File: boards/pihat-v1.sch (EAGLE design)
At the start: 53 parts, among them J10 RASPBERRYPI-40-PIN-GPIO_PTH_N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, Q1 BSS138, Q13 BSS138, Q2 BSS138, Q3 BSS138

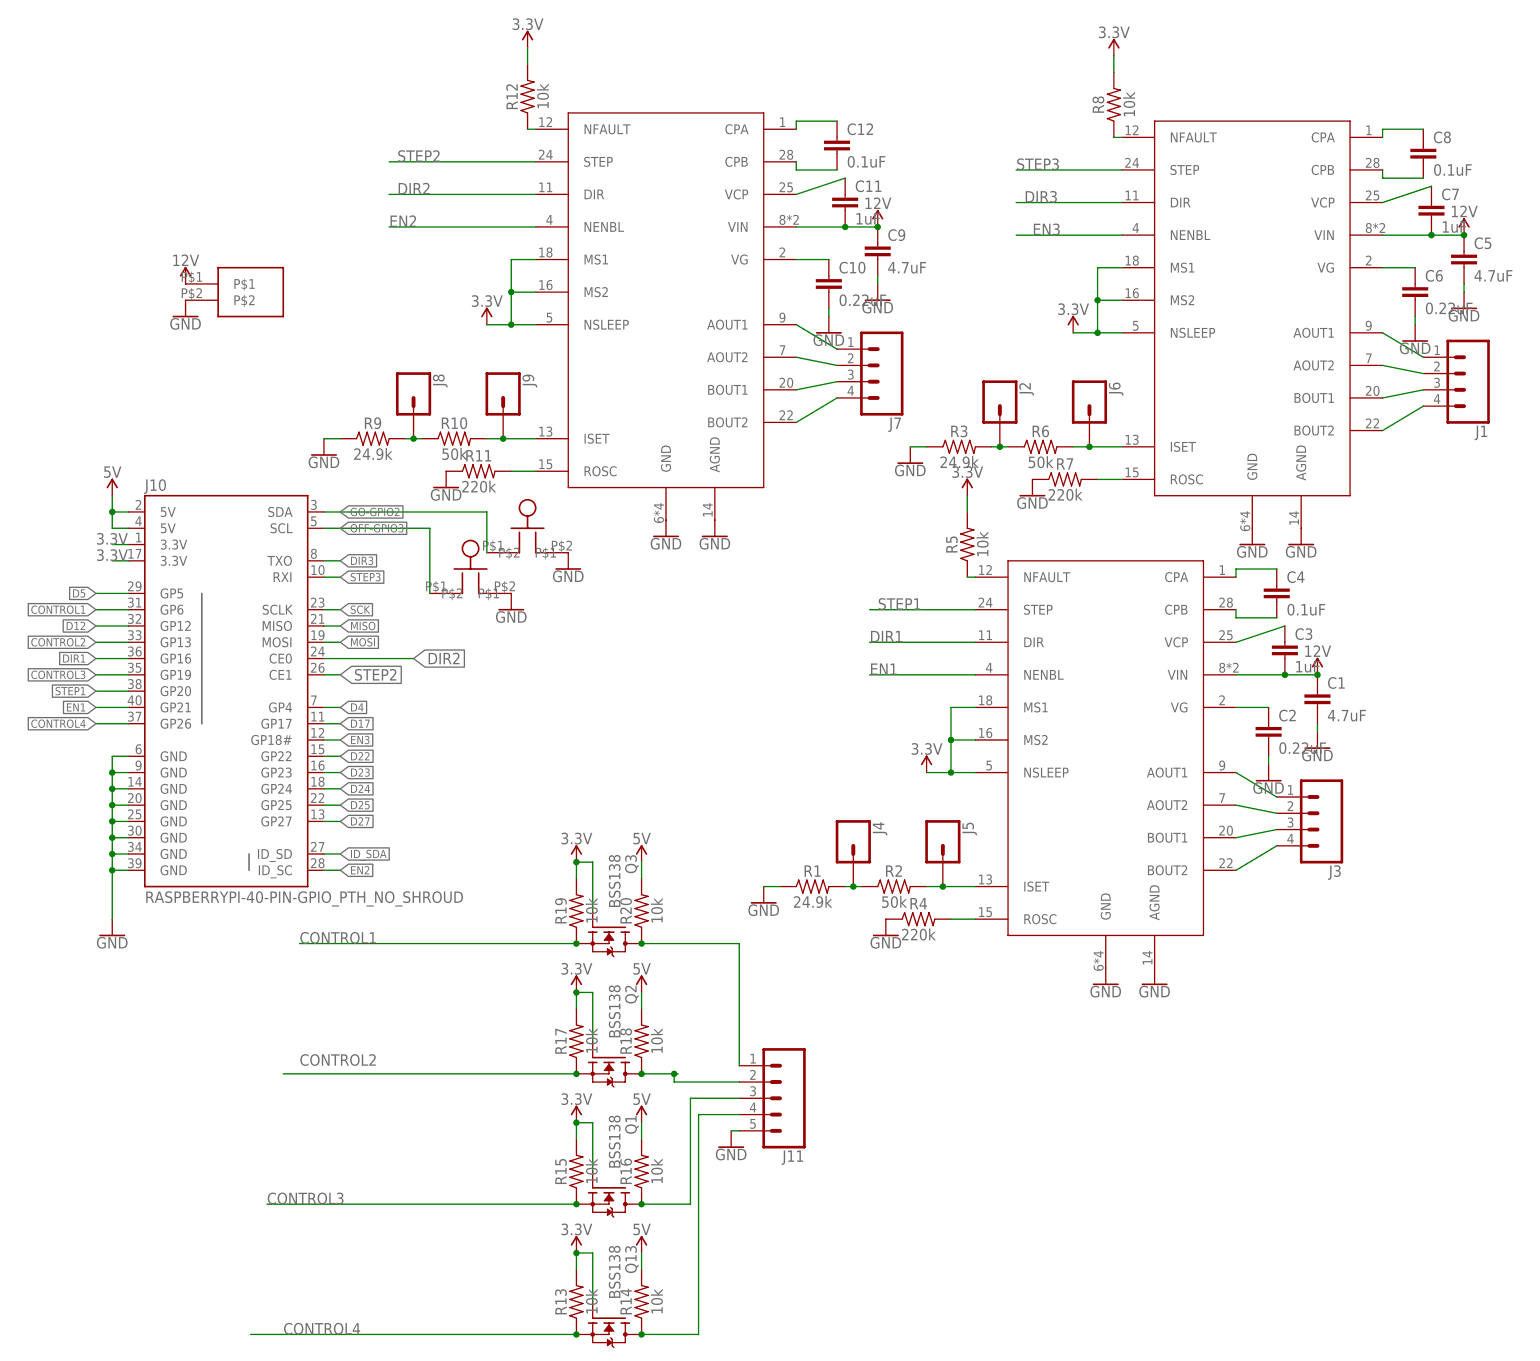
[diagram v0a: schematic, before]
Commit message: pihat streamlined, largely laid out
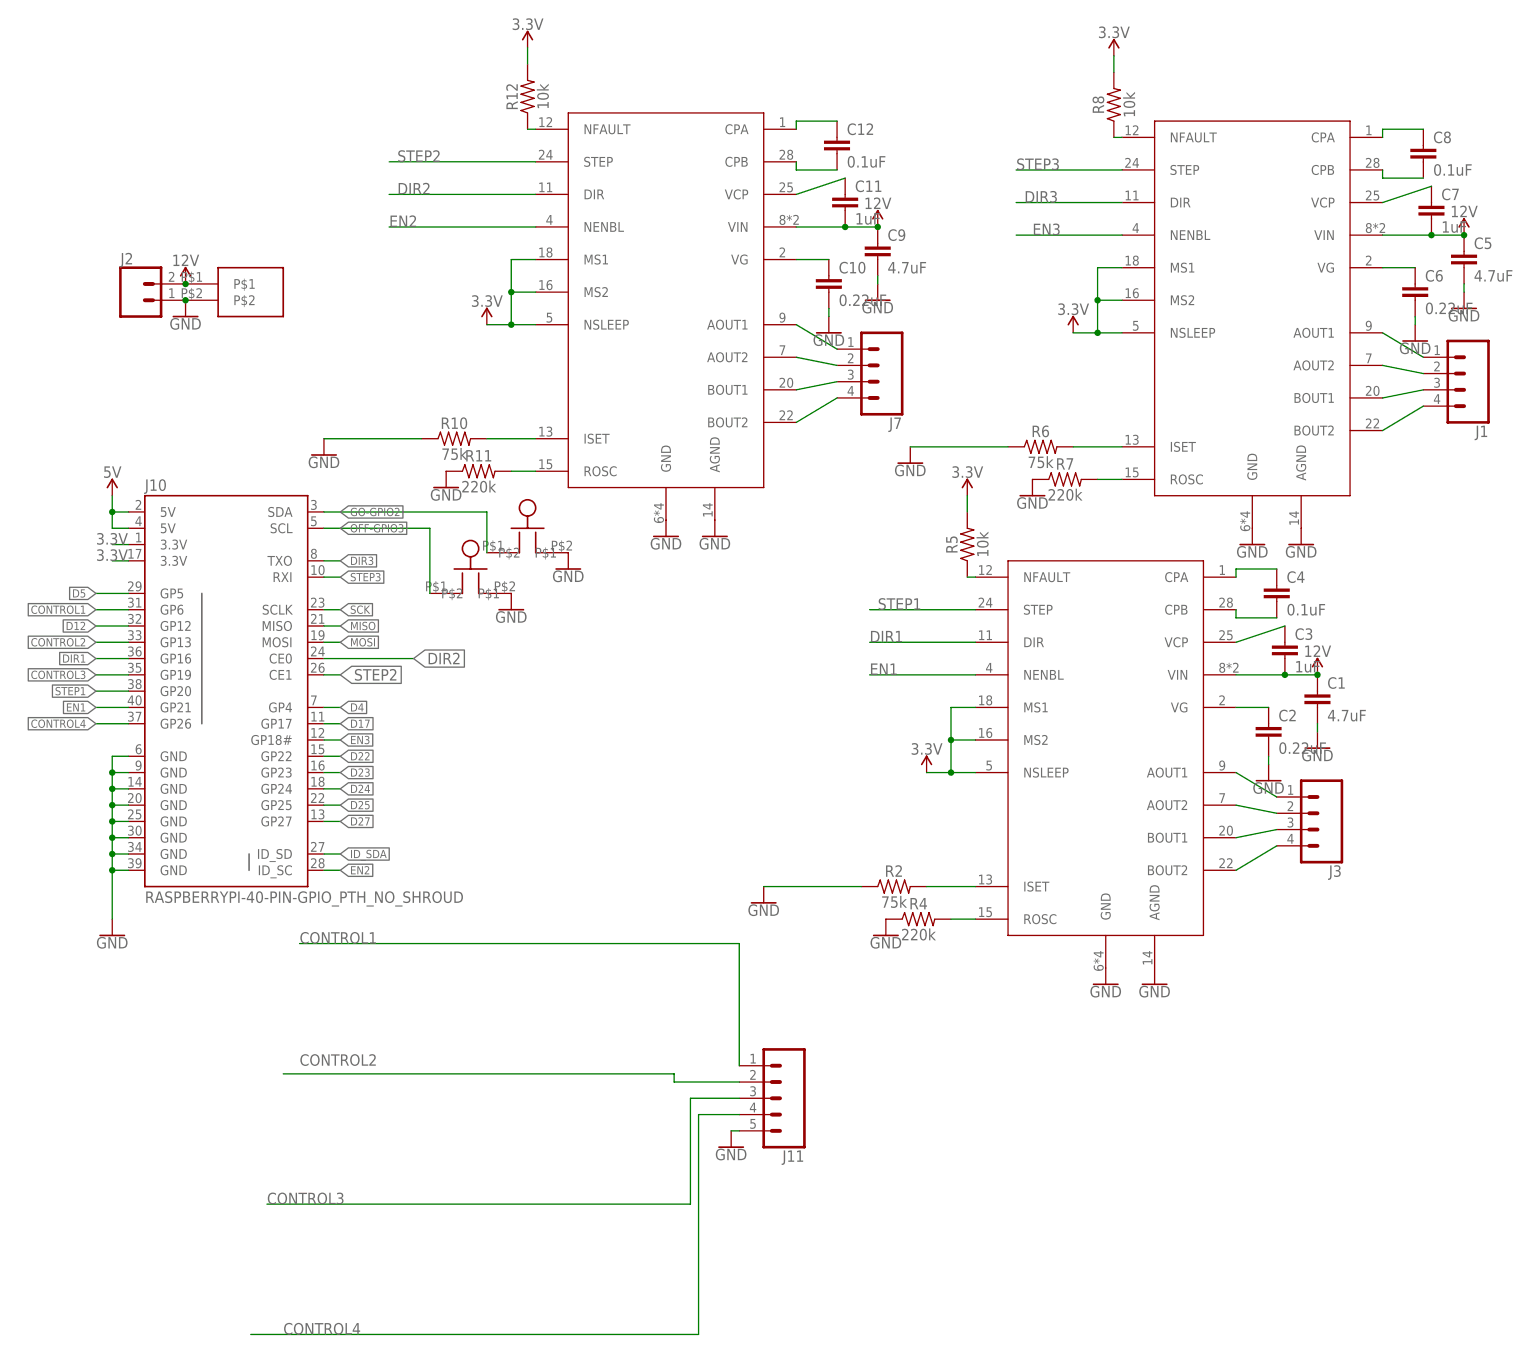
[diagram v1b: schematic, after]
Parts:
- removed J4, J5, J6, J8, J9: (no value), SparkFun-Connectors:CONN_01
- removed Q1, Q13, Q2, Q3: BSS138, bss138_10:BSS138
- removed R1, R3, R9: 24.9k, SparkFun-Resistors:10KOHM-0603-1/10W-1%
- removed R13, R14, R15, R16, R17, R18, R19, R20: 10k, SparkFun-Resistors:10KOHM-0603-1/10W-1%
- J2: device SparkFun-Connectors:CONN_01 -> SparkFun-Connectors:CONN_02
- R10, R2, R6: value 50k -> 75k
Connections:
- removed net N$26: J4.1, R1.2, R2.1
- removed net N$31: J2.1, R3.2, R6.1
- removed net N$48: J8.1, R10.1, R9.2
- removed net N$53: J11.1, Q3.D, R20.1
- removed net N$54: J11.2, Q2.D, R18.1
- removed net N$55: J11.3, Q1.D, R16.1
- removed net N$56: J11.4, Q13.D, R14.1
- net 12V: now also J2.2
- net 3.3V: no longer Q1.G, Q13.G, Q2.G, Q3.G, R13.2, R15.2, R17.2, R19.2
- net 5V: no longer R14.2, R16.2, R18.2, R20.2
- net CONTROL1: now also J11.1; no longer Q3.S, R19.1
- net CONTROL2: now also J11.2; no longer Q2.S, R17.1
- net CONTROL3: now also J11.3; no longer Q1.S, R15.1
- net CONTROL4: now also J11.4; no longer Q13.S, R13.1
- net GND: now also J2.1, R10.1, R2.1, R6.1; no longer R1.1, R3.1, R9.1
- net N$24: no longer J5.1
- net N$29: no longer J6.1
- net N$47: no longer J9.1
